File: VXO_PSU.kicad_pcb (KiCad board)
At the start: 4 copper layers, 199.4 x 40.6 mm, 47 parts, among them CON1 BARREL_JACK, P1 CONN_01X02, P10 CONN_02X08, P12 BNC, P13 BNC, P2 CONN_02X08, P3 CONN_02X08, P4 CONN_02X08, P5 CONN_02X08, P6 CONN_02X08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

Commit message: ordered prototype board with BNC connectors for testing
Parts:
- added HOLE-M3: VAL**, MyModules:HOLE-M3, F.Cu at (239.9, 111.7)
- added HOLE-M3: VAL**, MyModules:HOLE-M3, F.Cu at (132.7, 81.0)
- added HOLE-M3: VAL**, MyModules:HOLE-M3, F.Cu at (232.4, 81.0)
- added HOLE-M3: VAL**, MyModules:HOLE-M3, F.Cu at (232.4, 112.0)
- added HOLE-M3: VAL**, MyModules:HOLE-M3, F.Cu at (43.2, 81.0)
- added HOLE-M3: VAL**, MyModules:HOLE-M3, F.Cu at (43.2, 112.1)
- moved TP1 60.2 mm to (71.5, 114.2), turned to 90 degrees
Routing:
- net +12V: track 15.1 -> 18.0 mm, vias 10 -> 12

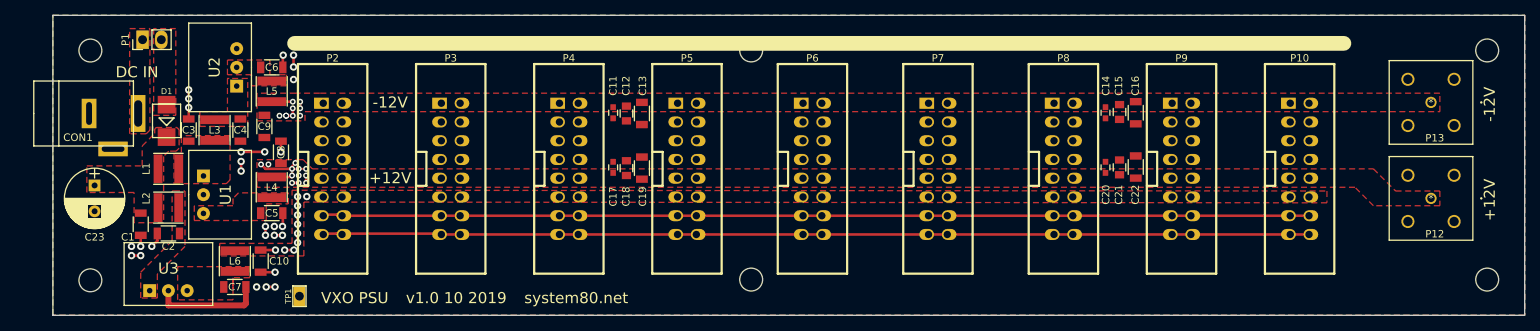
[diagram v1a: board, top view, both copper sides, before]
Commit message: added back negative rail pi filter, changed input L footprint
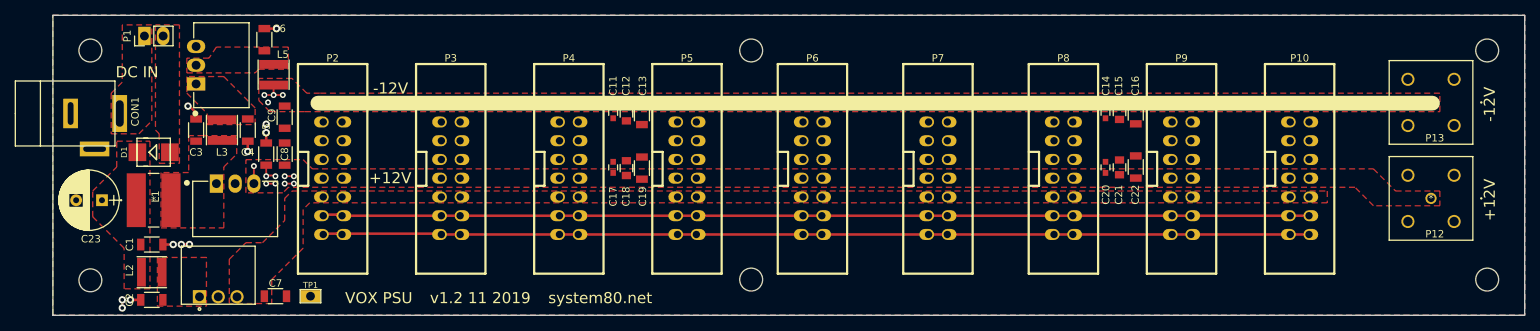
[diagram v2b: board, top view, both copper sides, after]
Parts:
- removed C10: 22µF, Capacitors_SMD:C_1206
- removed L4, L6: 10µH, Inductors_SMD:L_Taiyo-Yuden_NR-40xx
- C23: value CP_US -> 220µ
- L1: footprint Inductors_SMD:L_Taiyo-Yuden_NR-40xx -> MyModules:SRR6038-120Y
- L2: value 12µH -> 10µH
- U1, U2: value VX078-500 -> VX078012-1000; footprint MyModules:R-78E-0.5 -> MyModules:CONV_VXO78012-1000
- U3: footprint MyModules:R-78E-0.5 -> MyModules:CUI_VXO780XX-500
- moved C2 9.28 mm to (51.5, 114.8)
- moved L2 9.03 mm to (51.5, 111.0)
- moved C5 8.04 mm to (67.0, 95.0), turned to 90 degrees
- moved U3 7.98 mm to (60.5, 109.2), turned to 180 degrees
- moved U2 5.94 mm to (57.5, 85.5)
- moved C7 5.64 mm to (68.2, 114.2)
- moved L1 4.70 mm to (51.8, 101.2)
- moved D1 4.60 mm to (51.8, 94.8), turned to 0 degrees
- moved C6 3.88 mm to (66.8, 79.5), turned to 270 degrees
- moved C1 3.13 mm to (51.5, 107.2), turned to 0 degrees
- moved C9 3.02 mm to (69.5, 90.0)
- moved CON1 2.50 mm to (43.8, 89.5)
- moved U1 2.30 mm to (60.2, 99.0), turned to 0 degrees
- moved L5 2.26 mm to (68.0, 84.2)
- moved C23 2.24 mm to (44.8, 101.2), turned to 180 degrees
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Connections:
- C5 pad 1: Net-(C5-Pad1) -> +12V
- C7 pad 1: Net-(C7-Pad1) -> +5V
- U1 pad 3: Net-(C5-Pad1) -> +12V
- U3 pad 3: Net-(C7-Pad1) -> +5V
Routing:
- net GND: track 57.3 -> 15.1 mm, vias 27 -> 11
- net +5V: track 13.2 -> 0.00 mm, vias 10 -> 0
- net +12V: track 18.0 -> 13.6 mm, vias 12 -> 9
- net -12V: track 9.55 -> 6.31 mm, vias 9 -> 4
- net (no net): track 1.20 -> 0.00 mm
- removed copper zone on F.Cu, net Net-(C5-Pad1)
- removed copper zone on F.Cu, net Net-(C7-Pad1)
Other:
- board text added: "VOX PSU"
- board text added: "v1.2 11 2019"
- board text removed: "VXO PSU"
- board text removed: "v1.0 10 2019"

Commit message: VOX PSU renamed. few more tweaks then ready for PCB ordering
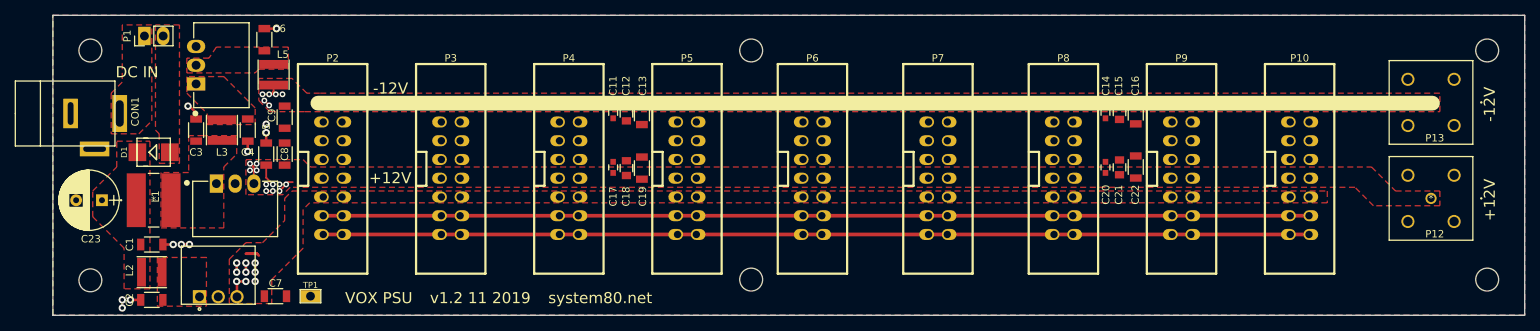
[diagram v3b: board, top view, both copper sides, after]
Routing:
- net +5V: track 0.00 -> 18.7 mm, vias 0 -> 9
- net +12V: track 13.6 -> 16.6 mm, vias 9 -> 11
- net -12V: track 6.31 -> 7.93 mm, vias 4 -> 6
- net /CV: track 134.3 -> 133.5 mm
- net /GATE: track 134.3 -> 133.7 mm
